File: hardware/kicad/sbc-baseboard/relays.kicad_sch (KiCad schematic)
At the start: 30 parts, among them J11 COM/NO/NC, J12 COM/NO/NC, J18 PSU in (isolated), J19 PSU out (isolated), K801 G6K-2F-Y DC5, K802 G6K-2F-Y DC5, K803 JW1FSN-DC5V, Q801 2N7002, Q802 2N7002, Q803 AO3400A, U801 LTV-817

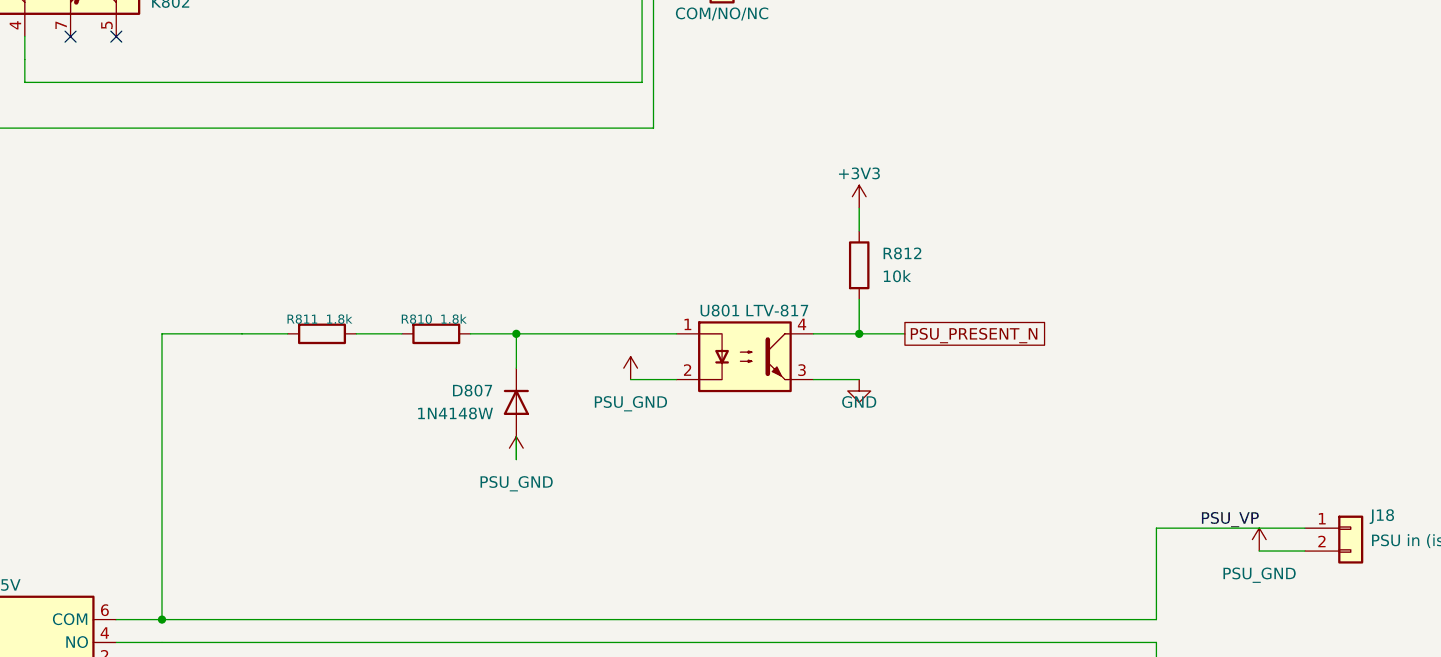
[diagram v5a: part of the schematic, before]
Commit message: First board: generated placement from the layout directives; current classes on the sheets
gen/pcb.py (pcbnew) builds sbc-baseboard.kicad_pcb once from the netlist, the
project file and gen/layout.py (docs/layout-directives.md as data): 140 x 80
outline with 2 mm corners, M3 holes on GND with corner keep-outs, the Advanced
Circuits 4-layer stackup, every footprint with its nets, edge connectors facing
outward (USB-C on their footprint's PCB Edge mark), interior parts packed by
function next to their connectors, the L2 ground plane with an isolated PSU_GND
island, and sbc-baseboard.kicad_dru with the passthrough's keep-out and 2 mm
creepage rules. DRC: no errors but twelve inside the GCT USB-C footprints
(hole to shield pad 0.19 mm against the fab's 0.25), 499 unrouted; silk left
for layout. The project file now carries the fab's constraints and the classes
PSU_3A, USB_VBUS_3A, PWR_6A, PSU_ISO; net class directive flags mark every
high-current net on the sheets; the opto's sense nets are named.

Directives revised at layout: J17 top-entry inboard (the RJ45 measures 22 mm),
J19 beside J18 (one compact isolated region), J9 on the right edge.

Co-Authored-By: Claude Fable 5.1 <noreply@anthropic.com>
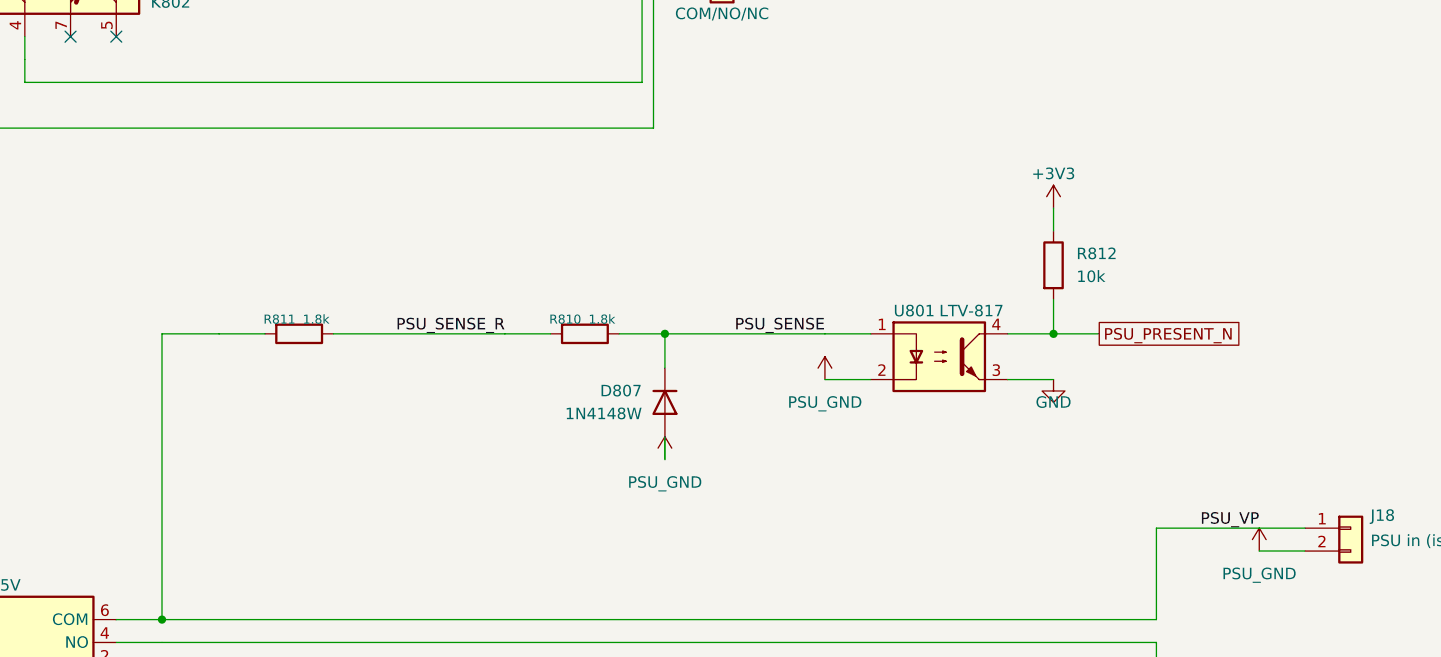
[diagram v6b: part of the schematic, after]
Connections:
- net PSU_SENSE: now reaches D807.1 (K), R810.1, U801.1
- net PSU_SENSE_R: now reaches R810.2, R811.1
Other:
- moved on the sheet: D807, R810, R811, R812, U801

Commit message: The PD inlet and the two 5 V bucks go; a 2.5 mm barrel jack feeds one +5V rail through a reverse-polarity FET
Power in is a 5 V 4 A (20 W) adapter on a Kycon KLDX-0202-BC barrel
jack (J2, centre positive), clamped by an SMAJ5.0A, passed by a
DMP3013SFV P-channel MOSFET (body diode toward the rail, gate at GND,
9.5 mOhm) into +5V: two 47 uF and a 100 nF, an amber LED. The
STUSB4500, its I2C buffer and Qwiic programming header, the two
TPS54560B bucks and their islands, VBUS_IN, +5V_PORTS and +5V_TGT as
separate rails are gone; +5V feeds the port switches, the relays, the
FTDI switch, the 3V3 buck and the TPS26630 eFuse, whose output is the
switched target rail +5V_TGT, now limited to 3 A (RILIM 6.04k, the
datasheet's 18 kOhm.A / IOL). The K64's I2C0 and PD pins are freed.
Classes: PWR_4A (2.5 mm, 1.0 mm vias) for +5V and +5V_TGT in place of
PWR_6A; USB_VBUS_3A keeps the port and FTDI VBUS nets. The directives
anchor the FET behind the jack, drop the bucks' and the PD controller's
templates, and draw the one +5V rail on L4 from the jack to the eFuse.
ERC clean; the placement passes every gate, 481 connections to route.

Co-Authored-By: Claude Fable 5.1 <noreply@anthropic.com>
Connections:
- net +5V_PORTS renamed +5V
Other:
- moved on the sheet: D805, D806, R807
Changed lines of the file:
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@@
 			)
 		)
-		(property "Value" "+5V_PORTS"
+		(property "Value" "+5V"
 			(at 139.7 60.96 0)
 			(show_name no)
@@
 			)
 		)
-		(property "Value" "+5V_PORTS"
+		(property "Value" "+5V"
 			(at 129.54 67.31 0)
 			(show_name no)
@@
 			)
 		)
-		(property "Value" "+5V_PORTS"
+		(property "Value" "+5V"
 			(at 114.3 60.96 0)
 			(show_name no)
@@
 			)
 		)
-		(property "Value" "+5V_PORTS"
+		(property "Value" "+5V"
 			(at 139.7 135.89 0)
 			(show_name no)
@@
 			)
 		)
-		(property "Value" "+5V_PORTS"
+		(property "Value" "+5V"
 			(at 129.54 142.24 0)
 			(show_name no)
@@
 			)
 		)
-		(property "Value" "+5V_PORTS"
+		(property "Value" "+5V"
 			(at 114.3 135.89 0)
 			(show_name no)
@@
 			)
 		)
-		(property "Value" "+5V_PORTS"
+		(property "Value" "+5V"
 			(at 132.08 218.44 0)
 			(show_name no)
@@
 		(pts
 			(xy 137.16 224.79)
-			(xy 116.84 224.79)
+			(xy 123.19 224.79)
 		)
 		(stroke
@@
 	(symbol
 		(lib_id "Diode:1N4148W")
-		(at 116.84 217.17 270)
+		(at 123.19 217.17 270)
 		(unit 1)
 		(body_style 1)
@@
 		(fields_autoplaced no)
 		(property "Reference" "D805"
-			(at 114.3 215.9 90)
+			(at 120.65 215.9 90)
 			(show_name no)
 			(do_not_autoplace no)
@@
 		)
 		(property "Value" "1N4148W"
-			(at 114.3 218.44 90)
+			(at 120.65 218.44 90)
 			(show_name no)
 			(do_not_autoplace no)
@@
 		)
 		(property "Footprint" "Diode_SMD:D_SOD-123"
-			(at 116.84 217.17 0)
+			(at 123.19 217.17 0)
 			(hide yes)
 			(show_name no)
@@
 		)
 		(property "Datasheet" "~"
-			(at 116.84 217.17 0)
+			(at 123.19 217.17 0)
 			(hide yes)
 			(show_name no)
@@
 		)
 		(property "Description" "75V 0.15A Fast Switching Diode, SOD-123"
-			(at 116.84 217.17 0)
+			(at 123.19 217.17 0)
 			(hide yes)
 			(show_name no)
@@
 	(wire
 		(pts
-			(xy 116.84 224.79)
-			(xy 116.84 220.98)
+			(xy 123.19 224.79)
+			(xy 123.19 220.98)
 		)
 		(stroke
@@
 	(wire
 		(pts
-			(xy 116.84 213.36)
-			(xy 116.84 210.82)
+			(xy 123.19 213.36)
+			(xy 123.19 210.82)
 		)
 		(stroke
@@
 	(symbol
 		(lib_id "power:+5V")
-		(at 116.84 210.82 0)
+		(at 123.19 210.82 0)
 		(unit 1)
 		(body_style 1)
@@
 		(fields_autoplaced no)
 		(property "Reference" "#PWR09012"
-			(at 116.84 210.82 0)
+			(at 123.19 210.82 0)
 			(hide yes)
 			(show_name no)
@@
 			)
 		)
-		(property "Value" "+5V_PORTS"
-			(at 116.84 207.01 0)
+		(property "Value" "+5V"
+			(at 123.19 207.01 0)
 			(show_name no)
 			(do_not_autoplace no)
@@
 		)
 		(property "Footprint" ""
-			(at 116.84 210.82 0)
+			(at 123.19 210.82 0)
 			(hide yes)
 			(show_name no)
@@
 		)
 		(property "Datasheet" "~"
-			(at 116.84 210.82 0)
+			(at 123.19 210.82 0)
 			(hide yes)
 			(show_name no)
@@
 		)
 		(property "Description" "Power symbol creates a global label with name \"+5V\""
-			(at 116.84 210.82 0)
+			(at 123.19 210.82 0)
 			(hide yes)
 			(show_name no)
@@
 	)
 	(junction
-		(at 116.84 224.79)
+		(at 123.19 224.79)
 		(diameter 0)
 		(color 0 0 0 0)
@@
 	(wire
 		(pts
-			(xy 116.84 224.79)
-			(xy 101.6 224.79)
+			(xy 123.19 224.79)
+			(xy 107.95 224.79)
 		)
 		(stroke
@@
 	(symbol
 		(lib_id "Device:LED")
-		(at 101.6 219.71 90)
+		(at 107.95 219.71 90)
 		(unit 1)
 		(body_style 1)
@@
 		(fields_autoplaced no)
 		(property "Reference" "D806"
-			(at 99.06 218.44 90)
+			(at 105.41 218.44 90)
 			(show_name no)
 			(do_not_autoplace no)
@@
 		)
 		(property "Value" "LED RED"
-			(at 99.06 220.98 90)
+			(at 105.41 220.98 90)
 			(show_name no)
 			(do_not_autoplace no)
@@
 		)
 		(property "Footprint" "LED_SMD:LED_0603_1608Metric"
-			(at 101.6 219.71 0)
+			(at 107.95 219.71 0)
 			(hide yes)
 			(show_name no)
@@
 		)
 		(property "Datasheet" "~"
-			(at 101.6 219.71 0)
+			(at 107.95 219.71 0)
 			(hide yes)
 			(show_name no)
@@
 		)
 		(property "Description" "Light emitting diode"
-			(at 101.6 219.71 0)
+			(at 107.95 219.71 0)
 			(hide yes)
 			(show_name no)
@@
 	(symbol
 		(lib_id "Device:R")
-		(at 101.6 210.82 0)
+		(at 107.95 210.82 0)
 		(unit 1)
 		(body_style 1)
@@
 		(fields_autoplaced no)
 		(property "Reference" "R807"
-			(at 99.06 209.55 0)
+			(at 105.41 209.55 0)
 			(show_name no)
 			(do_not_autoplace no)
@@
 		)
 		(property "Value" "2.2k"
-			(at 99.06 212.09 0)
+			(at 105.41 212.09 0)
 			(show_name no)
 			(do_not_autoplace no)
@@
 		)
 		(property "Footprint" "Resistor_SMD:R_0603_1608Metric"
-			(at 101.6 210.82 0)
+			(at 107.95 210.82 0)
 			(hide yes)
 			(show_name no)
@@
 		)
 		(property "Datasheet" "~"
-			(at 101.6 210.82 0)
+			(at 107.95 210.82 0)
 			(hide yes)
 			(show_name no)
@@
 		)
 		(property "Description" "Resistor"
-			(at 101.6 210.82 0)
+			(at 107.95 210.82 0)
 			(hide yes)
 			(show_name no)
@@
 	(wire
 		(pts
-			(xy 101.6 224.79)
-			(xy 101.6 223.52)
+			(xy 107.95 224.79)
+			(xy 107.95 223.52)
 		)
 		(stroke
@@
 	(wire
 		(pts
-			(xy 101.6 215.9)
-			(xy 101.6 214.63)
+			(xy 107.95 215.9)
+			(xy 107.95 214.63)
 		)
 		(stroke
@@
 	(wire
 		(pts
-			(xy 101.6 207.01)
-			(xy 101.6 204.47)
+			(xy 107.95 207.01)
+			(xy 107.95 204.47)
 		)
 		(stroke
@@
 	(symbol
 		(lib_id "power:+5V")
-		(at 101.6 204.47 0)
+		(at 107.95 204.47 0)
 		(unit 1)
 		(body_style 1)
@@
 		(fields_autoplaced no)
 		(property "Reference" "#PWR09013"
-			(at 101.6 204.47 0)
+			(at 107.95 204.47 0)
 			(hide yes)
 			(show_name no)
@@
 			)
 		)
-		(property "Value" "+5V_PORTS"
-			(at 101.6 200.66 0)
+		(property "Value" "+5V"
+			(at 107.95 200.66 0)
 			(show_name no)
 			(do_not_autoplace no)
@@
 		)
 		(property "Footprint" ""
-			(at 101.6 204.47 0)
+			(at 107.95 204.47 0)
 			(hide yes)
 			(show_name no)
@@
 		)
 		(property "Datasheet" "~"
-			(at 101.6 204.47 0)
+			(at 107.95 204.47 0)
 			(hide yes)
 			(show_name no)
@@
 		)
 		(property "Description" "Power symbol creates a global label with name \"+5V\""
-			(at 101.6 204.47 0)
+			(at 107.95 204.47 0)
 			(hide yes)
 			(show_name no)
@@
 	)
 	(junction
-		(at 101.6 224.79)
+		(at 107.95 224.79)
 		(diameter 0)
 		(color 0 0 0 0)
@@
 	(wire
 		(pts
-			(xy 101.6 224.79)
-			(xy 96.52 224.79)
+			(xy 107.95 224.79)
+			(xy 102.87 224.79)
 		)
 		(stroke
@@
 	(wire
 		(pts
-			(xy 96.52 224.79)
-			(xy 87.63 224.79)
+			(xy 102.87 224.79)
+			(xy 93.98 224.79)
 		)
 		(stroke
@@
 	(wire
 		(pts
-			(xy 87.63 224.79)
-			(xy 87.63 243.84)
+			(xy 93.98 224.79)
+			(xy 93.98 243.84)
 		)
 		(stroke
@@
 	(wire
 		(pts
-			(xy 87.63 243.84)
+			(xy 93.98 243.84)
 			(xy 72.39 243.84)
 		)
